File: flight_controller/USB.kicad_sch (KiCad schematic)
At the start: 11 parts, among them J17 TYPE-C16PIN2MD(073) (USB TYPE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, U15 SN74LVC1G07DBVR_C19829659

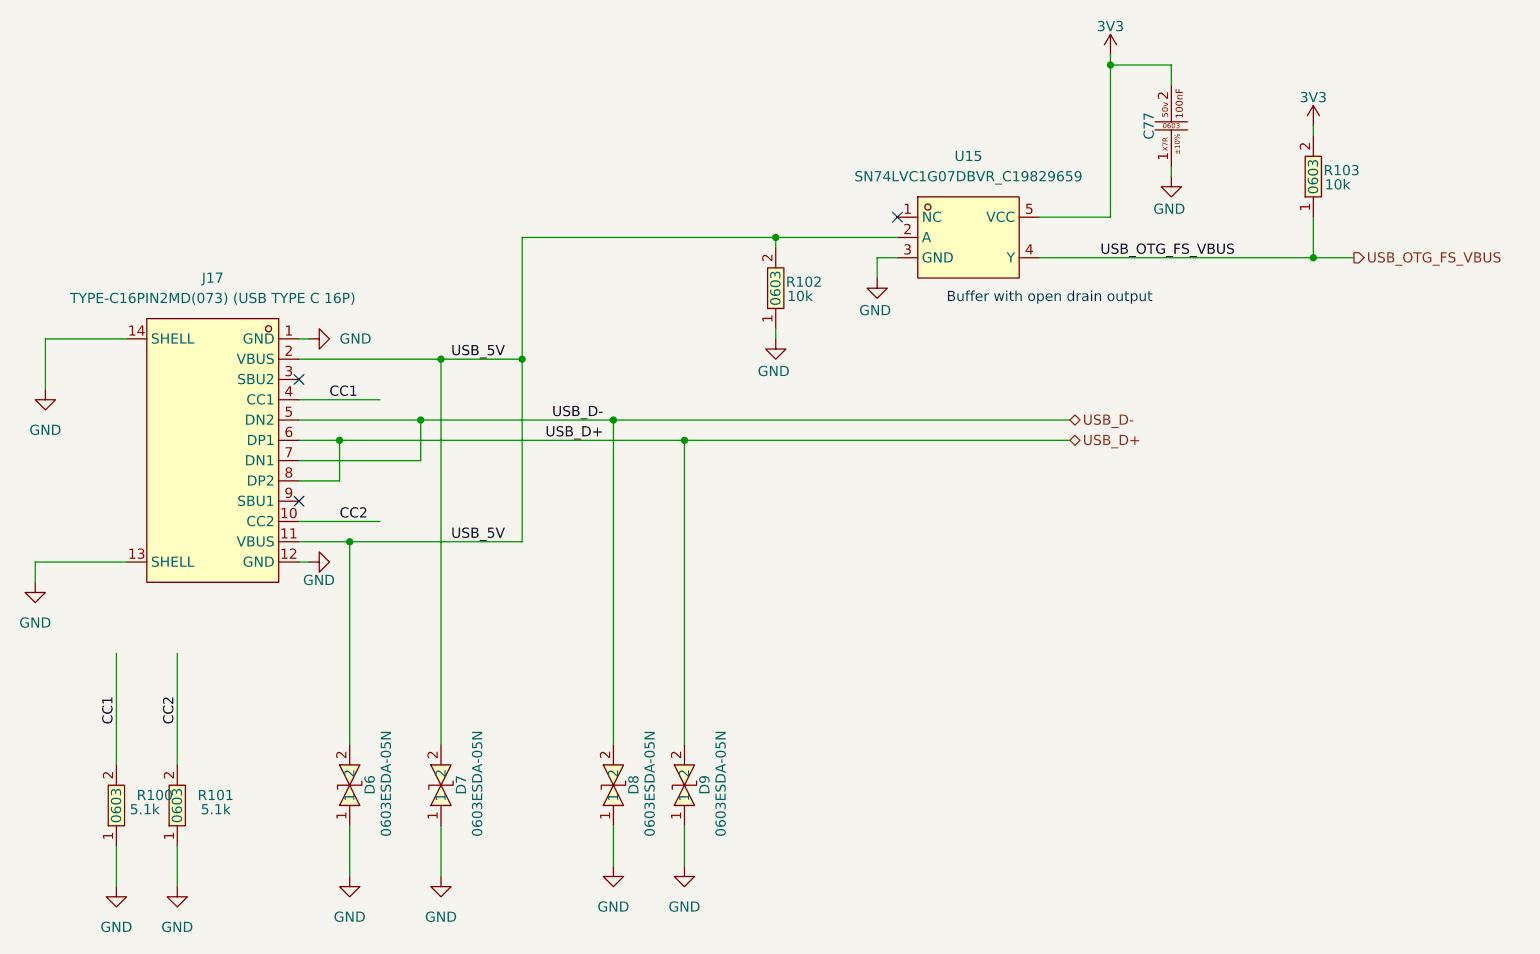
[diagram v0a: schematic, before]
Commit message: Updated power and usb connectors and netlist check
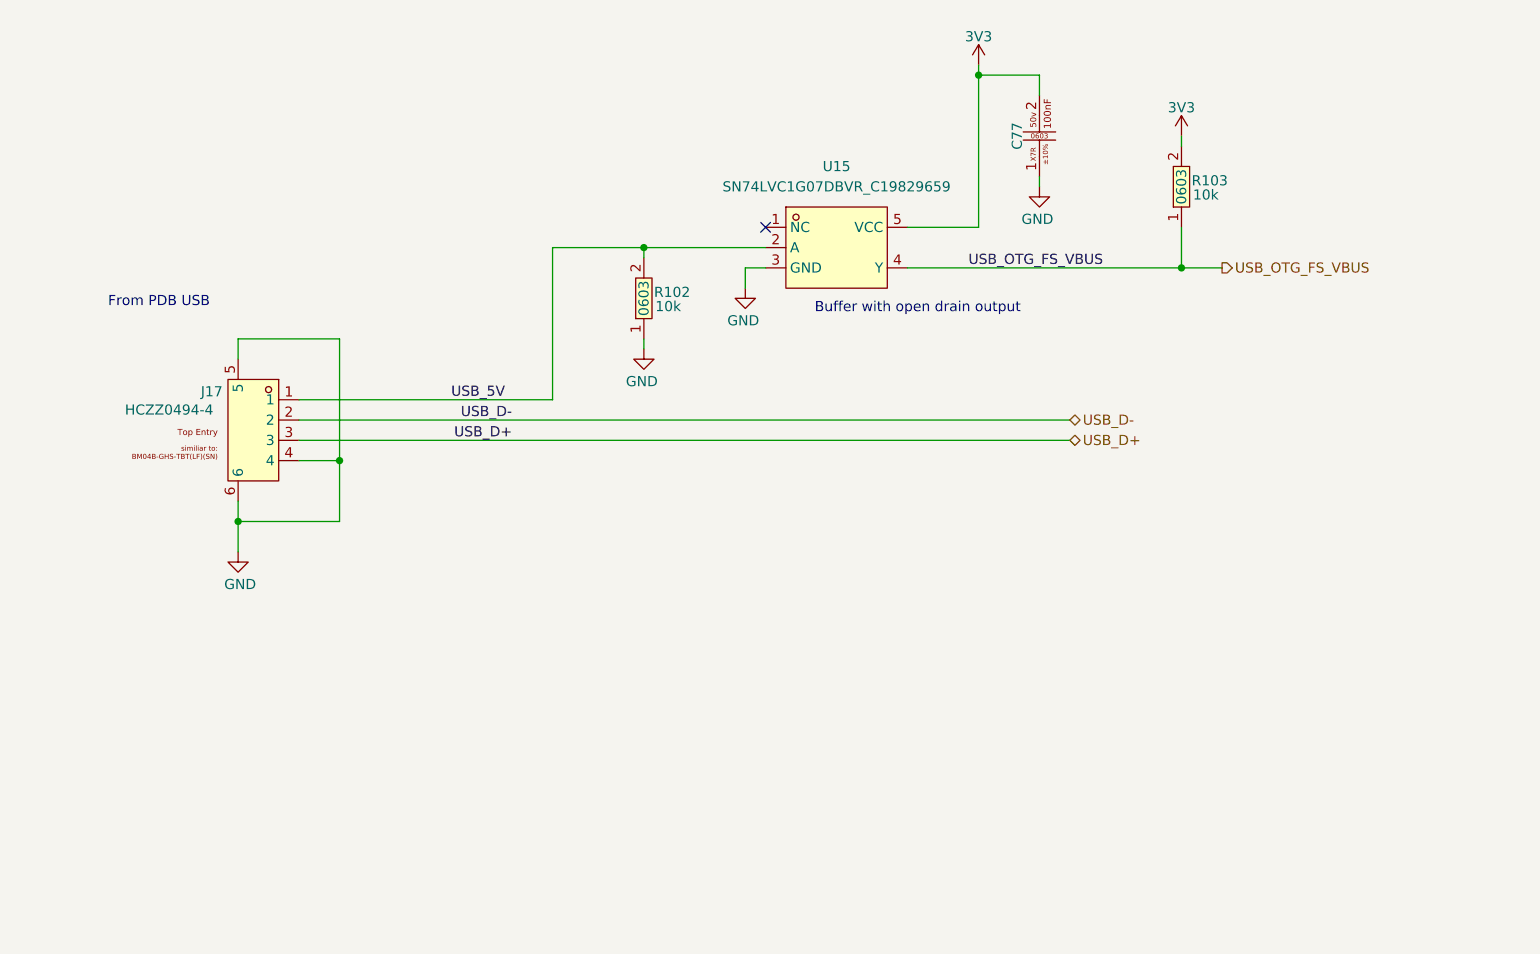
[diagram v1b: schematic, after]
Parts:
- removed D6, D7, D8, D9: 0603ESDA-05N, easyeda2kicad:D0603-BI, symbol easyeda2kicad:0603ESDA-05N
- removed J17: TYPE-C16PIN2MD(073) (USB TYPE C 16P), easyeda2kicad:USB-C-SMD_TYPE-C-6PIN-2MD-073, symbol lampelKicadLIB:TYPE-C16PIN2MD(073) (USB TYPE C 16P)
- removed R100, R101: 0603WAF5101T5E, easyeda2kicad:R0603, symbol easyeda2kicad:0603WAF5101T5E
- added J17: HCZZ0494-4, easyeda2kicad:CONN-SMD_4P-P1.25_BM04B-GHS-TBT-LF-SN, symbol lampelKicadLIB:HCZZ0494-4
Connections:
- net GND: now also J17.4, J17.5, J17.6
- net USB_5V: now also J17.1
- net USB_D+: now also J17.3
- net USB_D-: now also J17.2
- no-connect marks 3 -> 1
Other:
- note added: "From PDB USB"
- moved on the sheet: C77, R102, R103, U15
